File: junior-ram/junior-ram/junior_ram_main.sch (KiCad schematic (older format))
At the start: 1 part, among them IC5 GAL16V8

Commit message: junior ram
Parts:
- added IC6, IC7: 62256, elektor:DIL-28, symbol junior_computer:62256
- added IC8, IC9: 27C256, elektor:DIL-28, symbol Memory_EPROM:27C256
- added J2, J3: Conn_01x03_Male, elektor:CONN-3, symbol Connector:Conn_01x03_Male
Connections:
- net +5V: now also IC6.28 (VCC), IC7.28 (VCC), IC8.1 (VPP), IC8.28 (VCC), IC9.1 (VPP), IC9.28 (VCC), J2.3 (Pin_3), J3.3 (Pin_3)
- net AB11: now also IC5.5 (I5), IC6.23 (A11), IC7.23 (A11), IC8.23 (A11), IC9.23 (A11); no longer IC5.1 (I1/CLK)
- net AB12: now also IC5.3 (I3), IC6.2 (A12), IC7.2 (A12), IC8.2 (A12), IC9.2 (A12); no longer IC5.2 (I2)
- net AB13: now also IC5.4 (I4), IC6.26 (A13), IC7.26 (A13), IC8.26 (A13), IC9.26 (A13); no longer IC5.3 (I3)
- net AB14: now also IC5.1 (I1/CLK), IC6.1 (A14), IC7.1 (A14), J2.1 (Pin_1), J3.1 (Pin_1); no longer IC5.4 (I4)
- net AB15: now also IC5.2 (I2); no longer IC5.5 (I5)
- net GND: now also IC6.14 (GND), IC7.14 (GND), IC8.14 (GND), IC9.14 (GND)
- new net: IC8.27 (A14), J2.2 (Pin_2)
- new net: IC9.27 (A14), J3.2 (Pin_2)
- new net AB0: IC6.10 (A0), IC7.10 (A0), IC8.10 (A0), IC9.10 (A0)
- new net AB1: IC6.9 (A1), IC7.9 (A1), IC8.9 (A1), IC9.9 (A1)
- new net AB10: IC6.21 (A10), IC7.21 (A10), IC8.21 (A10), IC9.21 (A10)
- new net AB2: IC6.8 (A2), IC7.8 (A2), IC8.8 (A2), IC9.8 (A2)
- new net AB3: IC6.7 (A3), IC7.7 (A3), IC8.7 (A3), IC9.7 (A3)
- new net AB4: IC6.6 (A4), IC7.6 (A4), IC8.6 (A4), IC9.6 (A4)
- new net AB5: IC6.5 (A5), IC7.5 (A5), IC8.5 (A5), IC9.5 (A5)
- new net AB6: IC6.4 (A6), IC7.4 (A6), IC8.4 (A6), IC9.4 (A6)
- new net AB7: IC6.3 (A7), IC7.3 (A7), IC8.3 (A7), IC9.3 (A7)
- new net AB8: IC6.25 (A8), IC7.25 (A8), IC8.25 (A8), IC9.25 (A8)
- new net AB9: IC6.24 (A9), IC7.24 (A9), IC8.24 (A9), IC9.24 (A9)
- new net DB0: IC6.11 (D0), IC7.11 (D0), IC8.11 (D0), IC9.11 (D0)
- new net DB1: IC6.12 (D1), IC7.12 (D1), IC8.12 (D1), IC9.12 (D1)
- new net DB2: IC6.13 (D2), IC7.13 (D2), IC8.13 (D2), IC9.13 (D2)
- new net DB3: IC6.15 (D3), IC7.15 (D3), IC8.15 (D3), IC9.15 (D3)
- new net DB4: IC6.16 (D4), IC7.16 (D4), IC8.16 (D4), IC9.16 (D4)
- new net DB5: IC6.17 (D5), IC7.17 (D5), IC8.17 (D5), IC9.17 (D5)
- new net DB6: IC6.18 (D6), IC7.18 (D6), IC8.18 (D6), IC9.18 (D6)
- new net DB7: IC6.19 (D7), IC7.19 (D7), IC8.19 (D7), IC9.19 (D7)

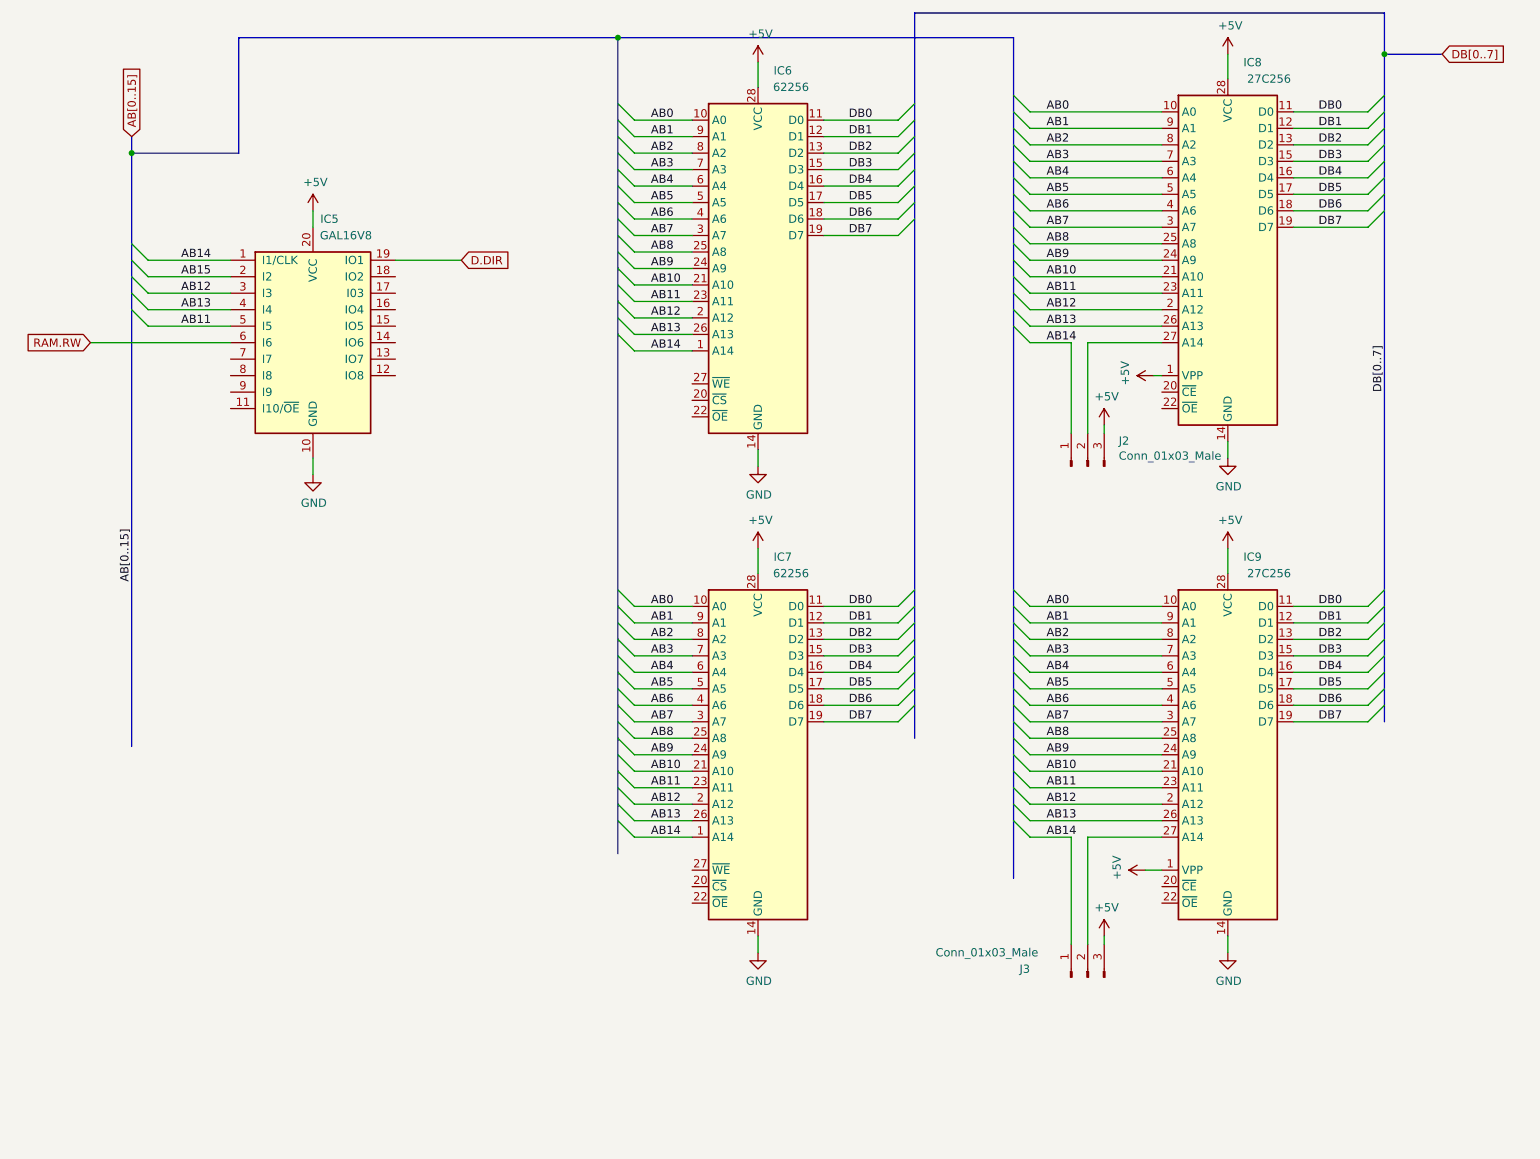
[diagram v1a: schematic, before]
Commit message: junior ram routage complet
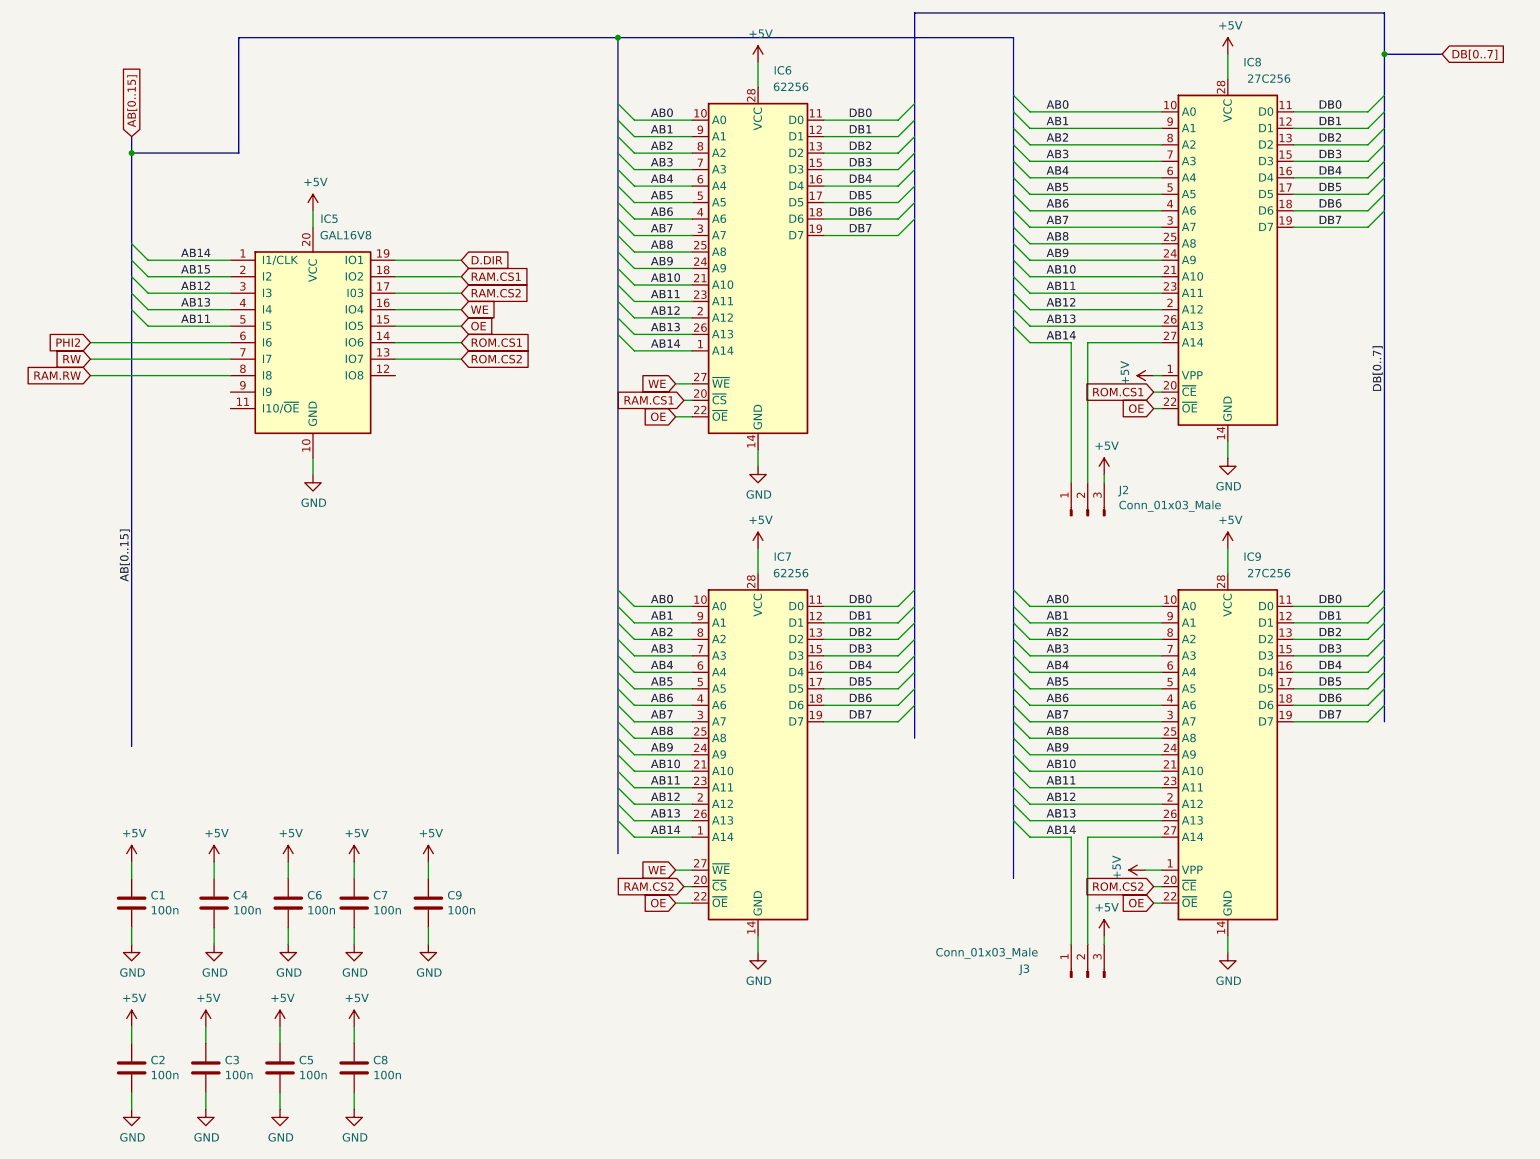
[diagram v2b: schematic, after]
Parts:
- added C1, C2, C3, C4, C5, C6, C7, C8, C9: 100n, elektor:CAP-2-HEX, symbol Device:C
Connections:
- net +5V: now also C1.1, C2.1, C3.1, C4.1, C5.1, C6.1, C7.1, C8.1, C9.1
- net GND: now also C1.2, C2.2, C3.2, C4.2, C5.2, C6.2, C7.2, C8.2, C9.2
- net RAM.RW: now also IC5.8 (I8); no longer IC5.6 (I6)
- net ROM.CS2: now reaches IC5.13 (IO7)
- net ROM.CS2: now also IC9.20 (~CE)
- net ROM.CS1: now reaches IC5.14 (IO6)
- net ROM.CS1: now also IC8.20 (~CE)
- net OE: now reaches IC5.15 (IO5)
- net OE: now also IC6.22 (~OE), IC7.22 (~OE), IC8.22 (~OE), IC9.22 (~OE)
- net WE: now reaches IC5.16 (IO4)
- net WE: now also IC6.27 (~WE), IC7.27 (~WE)
- net RAM.CS2: now reaches IC5.17 (I03)
- net RAM.CS2: now also IC7.20 (~CS)
- net RAM.CS1: now reaches IC5.18 (IO2)
- net RAM.CS1: now also IC6.20 (~CS)
- net RW: now reaches IC5.7 (I7)
- new net PHI2: IC5.6 (I6)
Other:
- moved on the sheet: J2
